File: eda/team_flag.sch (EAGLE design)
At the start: 22 parts, among them Q1 IRFML8244, Q2 IRFML8244, U1 ISL83491SOIC, U2 ATTINY1634

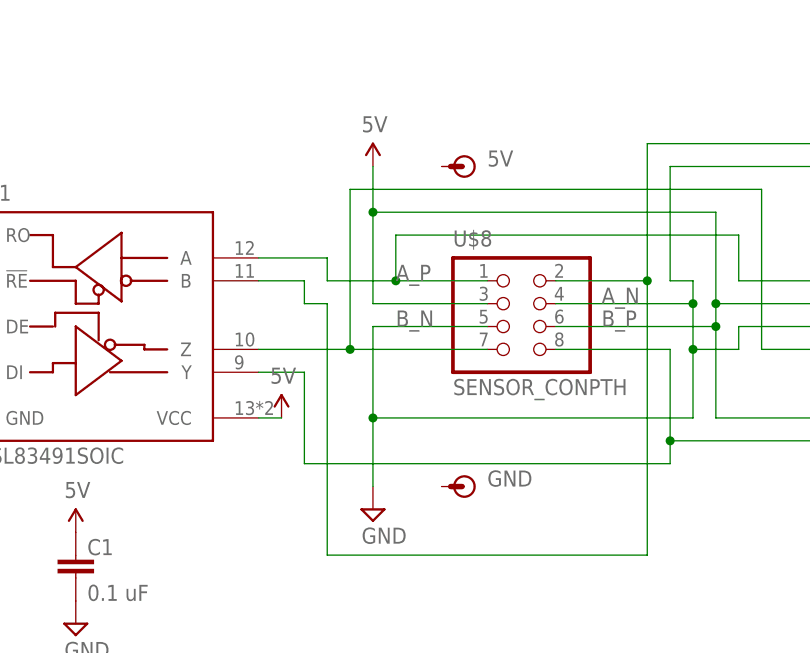
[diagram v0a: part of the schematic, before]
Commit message: Replaced 2x4 connectors with 2x5's.
On smartsensor, smartsensorPowered, smartsensor_powered_jig, and team_flag.
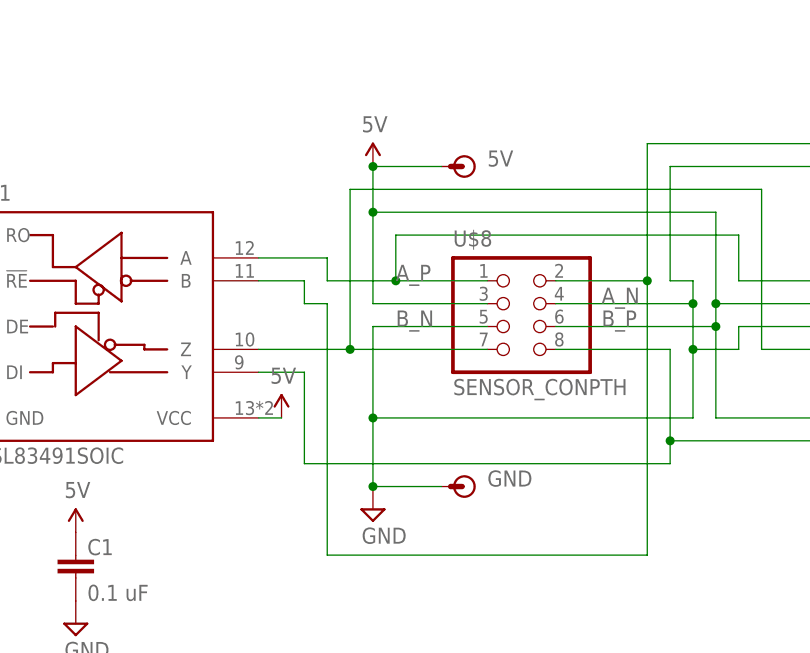
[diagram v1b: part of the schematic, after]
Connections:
- net 5V: now also 5V.P$1
- net GND: now also GND.P$1
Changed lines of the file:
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@@
 <pinref part="U$9" gate="G$1" pin="4"/>
 <wire x1="233.68" y1="137.16" x2="228.6" y2="137.16" width="0.1524" layer="91"/>
+<pinref part="GND" gate="G$1" pin="P$1"/>
+<wire x1="175.26" y1="116.84" x2="167.64" y2="116.84" width="0.1524" layer="91"/>
+<junction x="167.64" y="116.84"/>
 </segment>
 </net>
@@
 <pinref part="U$9" gate="G$1" pin="6"/>
 <wire x1="233.68" y1="134.62" x2="228.6" y2="134.62" width="0.1524" layer="91"/>
+<pinref part="5V" gate="G$1" pin="P$1"/>
+<wire x1="175.26" y1="152.4" x2="167.64" y2="152.4" width="0.1524" layer="91"/>
+<junction x="167.64" y="152.4"/>
 </segment>
 <segment>

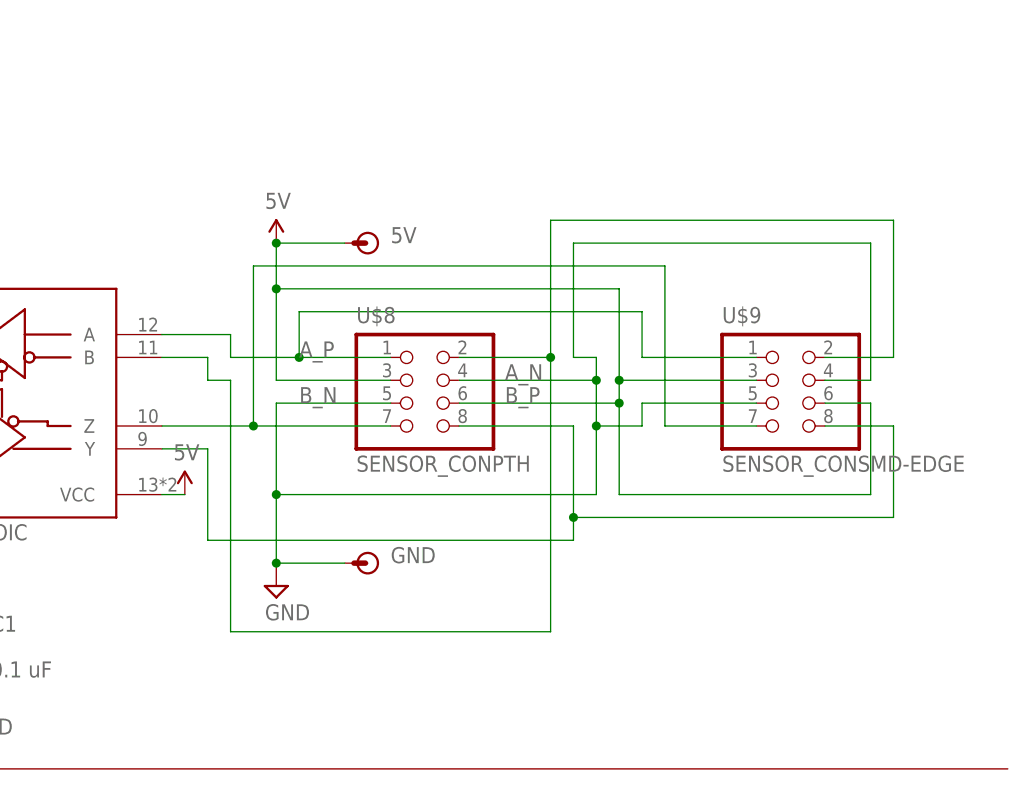
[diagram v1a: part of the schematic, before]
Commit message: Replaced 2x4 connector with 2x5 on team_flag.
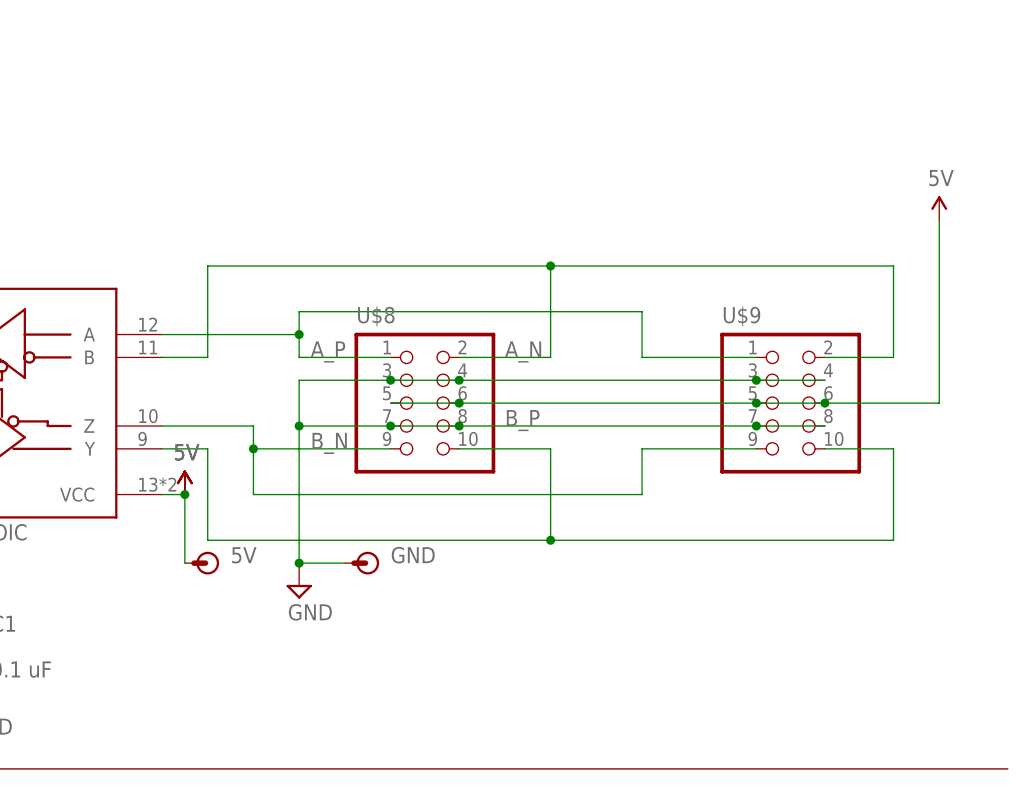
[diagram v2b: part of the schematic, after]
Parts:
- U$8: value SENSOR_CONPTH -> (none); device pie:SENSOR_CONPTH -> pie:SENSOR_CON_5PINPTH
- U$9: value SENSOR_CONSMD-EDGE -> (none); device pie:SENSOR_CONSMD-EDGE -> pie:SENSOR_CON_5PINSMD-EDGE
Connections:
- net 5V: now also U$8.5, U$9.5; no longer U$8.3, U$9.3
- net B_N: now also U$8.9, U$9.9; no longer U$8.7, U$9.7
- net B_P: now also U$8.10, U$9.10; no longer U$8.8, U$9.8
- net GND: now also U$8.3, U$8.7, U$8.8, U$9.3, U$9.7, U$9.8; no longer U$8.5, U$9.5
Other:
- moved on the sheet: 5V
